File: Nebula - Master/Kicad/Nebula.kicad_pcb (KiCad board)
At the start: 2 copper layers, 39.1 x 39.9 mm, 94 parts, among them J1 1054550101, J2 Display, M1 HMotor, Q1 s8050, Q2 C70022, Q3 s8050, SW1 SW_Push, SW2 SW_Push, SW3 SW_Push, U1 DRV5021, U10 MPU6050, U11 INMP441, U2 DRV5021, U3 DRV5021, U4 ESP32-S3-MINI-1-N8, U5 MCP73831T-2ATI/OT, U6 LTR-303ALS-01, U7 TPS61200DRC, U8 PCF8563TS, U9 MAX98357AETE, Y1 32.768KHz

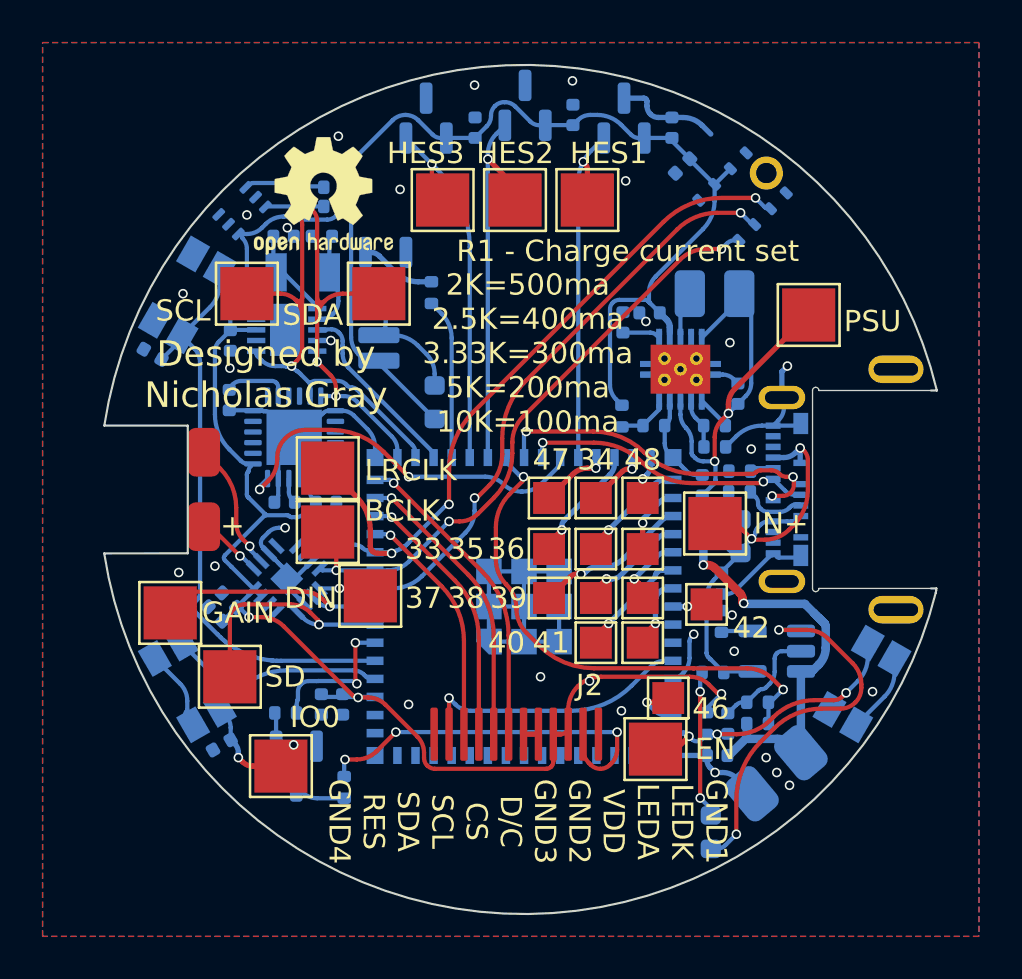
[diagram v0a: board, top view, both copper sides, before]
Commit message: Added BOM and minor changes
Fixed mosfet footprint and magnetic sensor footprints
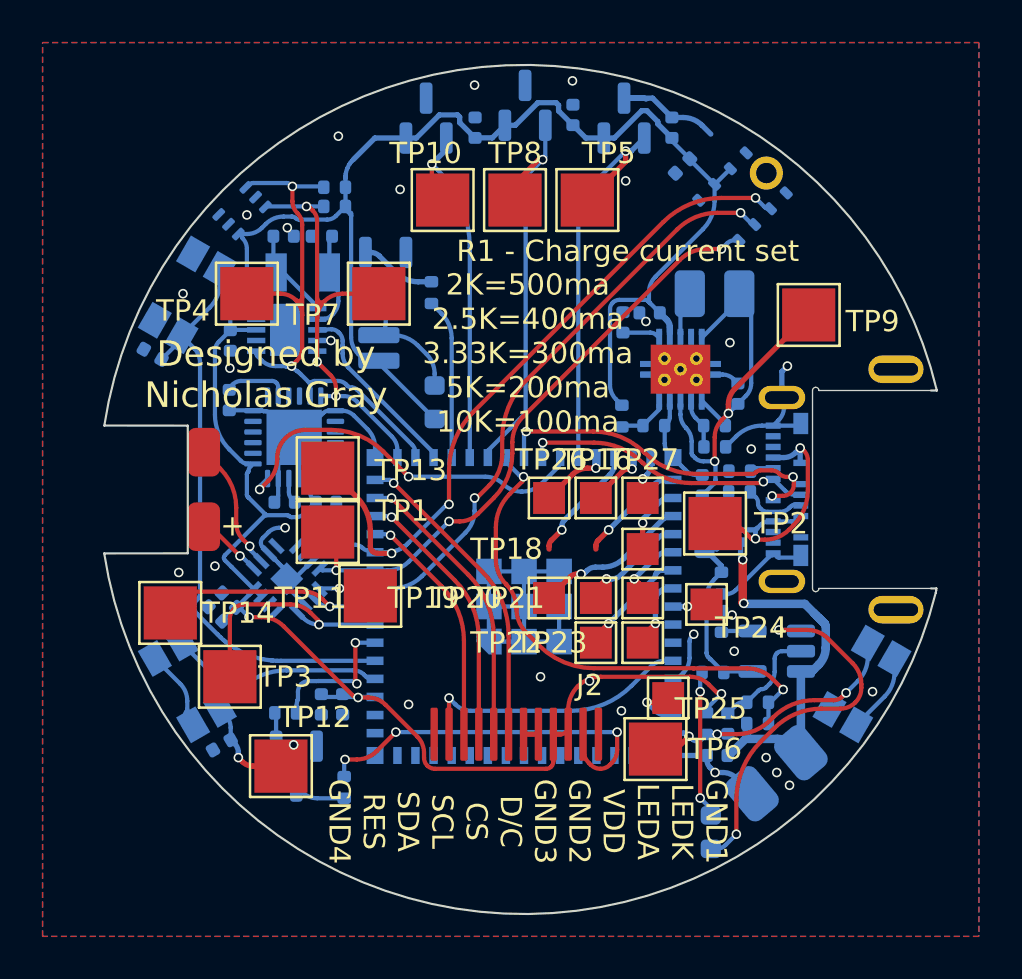
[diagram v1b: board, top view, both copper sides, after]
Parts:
- removed 33, 35: TestPoint, TestPoint:TestPoint_Pad_1.5x1.5mm
- removed REF**: OSHW-Logo2_7.3x6mm_SilkScreen, Symbol:OSHW-Logo2_7.3x6mm_SilkScreen
- Q2: value C70022 -> CJ3139K
- U1, U2, U3: value DRV5021 -> XC3202B183MR-G
- moved D2 1.71 mm to (164.1, 92.0)
- moved Q2 1.00 mm to (165.4, 91.9)
- renumbered BCLK to TP1, HES3 to TP10, DIN to TP11, IO0 to TP12, LRCLK to TP13, GAIN to TP14, 34 to TP16, 36 to TP18, 37 to TP19, IN+ to TP2, 38 to TP20, 39 to TP21, 40 to TP22, 41 to TP23, 42 to TP24, 46 to TP25, 47 to TP26, 48 to TP27, SD to TP3, SCL to TP4, HES1 to TP5, EN to TP6, SDA to TP7, HES2 to TP8, PSU to TP9
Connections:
- Q2 pad 1: VCC_IN -> +BATT
- Q2 pad 2: +BATT -> VCC_IN
- U1 pad 1: +3V3 -> HES1
- U1 pad 2: HES1 -> +3V3
- U2 pad 1: +3V3 -> HES2
- U2 pad 2: HES2 -> +3V3
- U3 pad 1: +3V3 -> HES3
- U3 pad 2: HES3 -> +3V3
- U4 pad 28: Net-(U4-Pad28) -> unconnected-(U4-Pad28)
- U4 pad 31: Net-(U4-Pad31) -> unconnected-(U4-Pad31)
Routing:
- net unconnected-(U4-Pad28): track 0.00 -> 5.50 mm, vias 0 -> 1
- net Net-(U4-Pad28): track 5.50 -> 0.00 mm, vias 1 -> 0
- net unconnected-(U4-Pad31): track 0.00 -> 5.09 mm, vias 0 -> 1
- net Net-(U4-Pad31): track 5.09 -> 0.00 mm, vias 1 -> 0
- net HES1: track 17.3 -> 19.5 mm
- net VCC_IN: track 22.9 -> 24.3 mm
- net +3V3: track 116.1 -> 117.2 mm
- net HES2: track 18.3 -> 19.3 mm
- net +BATT: track 18.4 -> 17.4 mm
- net GND: track 80.6 -> 81.4 mm
